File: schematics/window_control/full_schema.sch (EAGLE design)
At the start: 70 parts, among them IC1 MEGA32-P, J1 MTR-SERVO-FS5103B, J2 J2, J3 J2, J4 J2, J5 J2, J6 J2, J7 J2, J8 J2, J9 J2, Q1 2N3904, Q2 2N3904, Q3 2N3906BU, Q4 2N3904, Q5 STP14NM50N, SW1 SWITCH, U1 ESP32, U2 LM311P, U3 NE555P, U4 SN74LS32N, U5 BMP280 / 5V, U7 VOLTAGE_REGULATOR, U8 GY-SGP30, U9 LM358, X1 HC-49S (16MHZ)

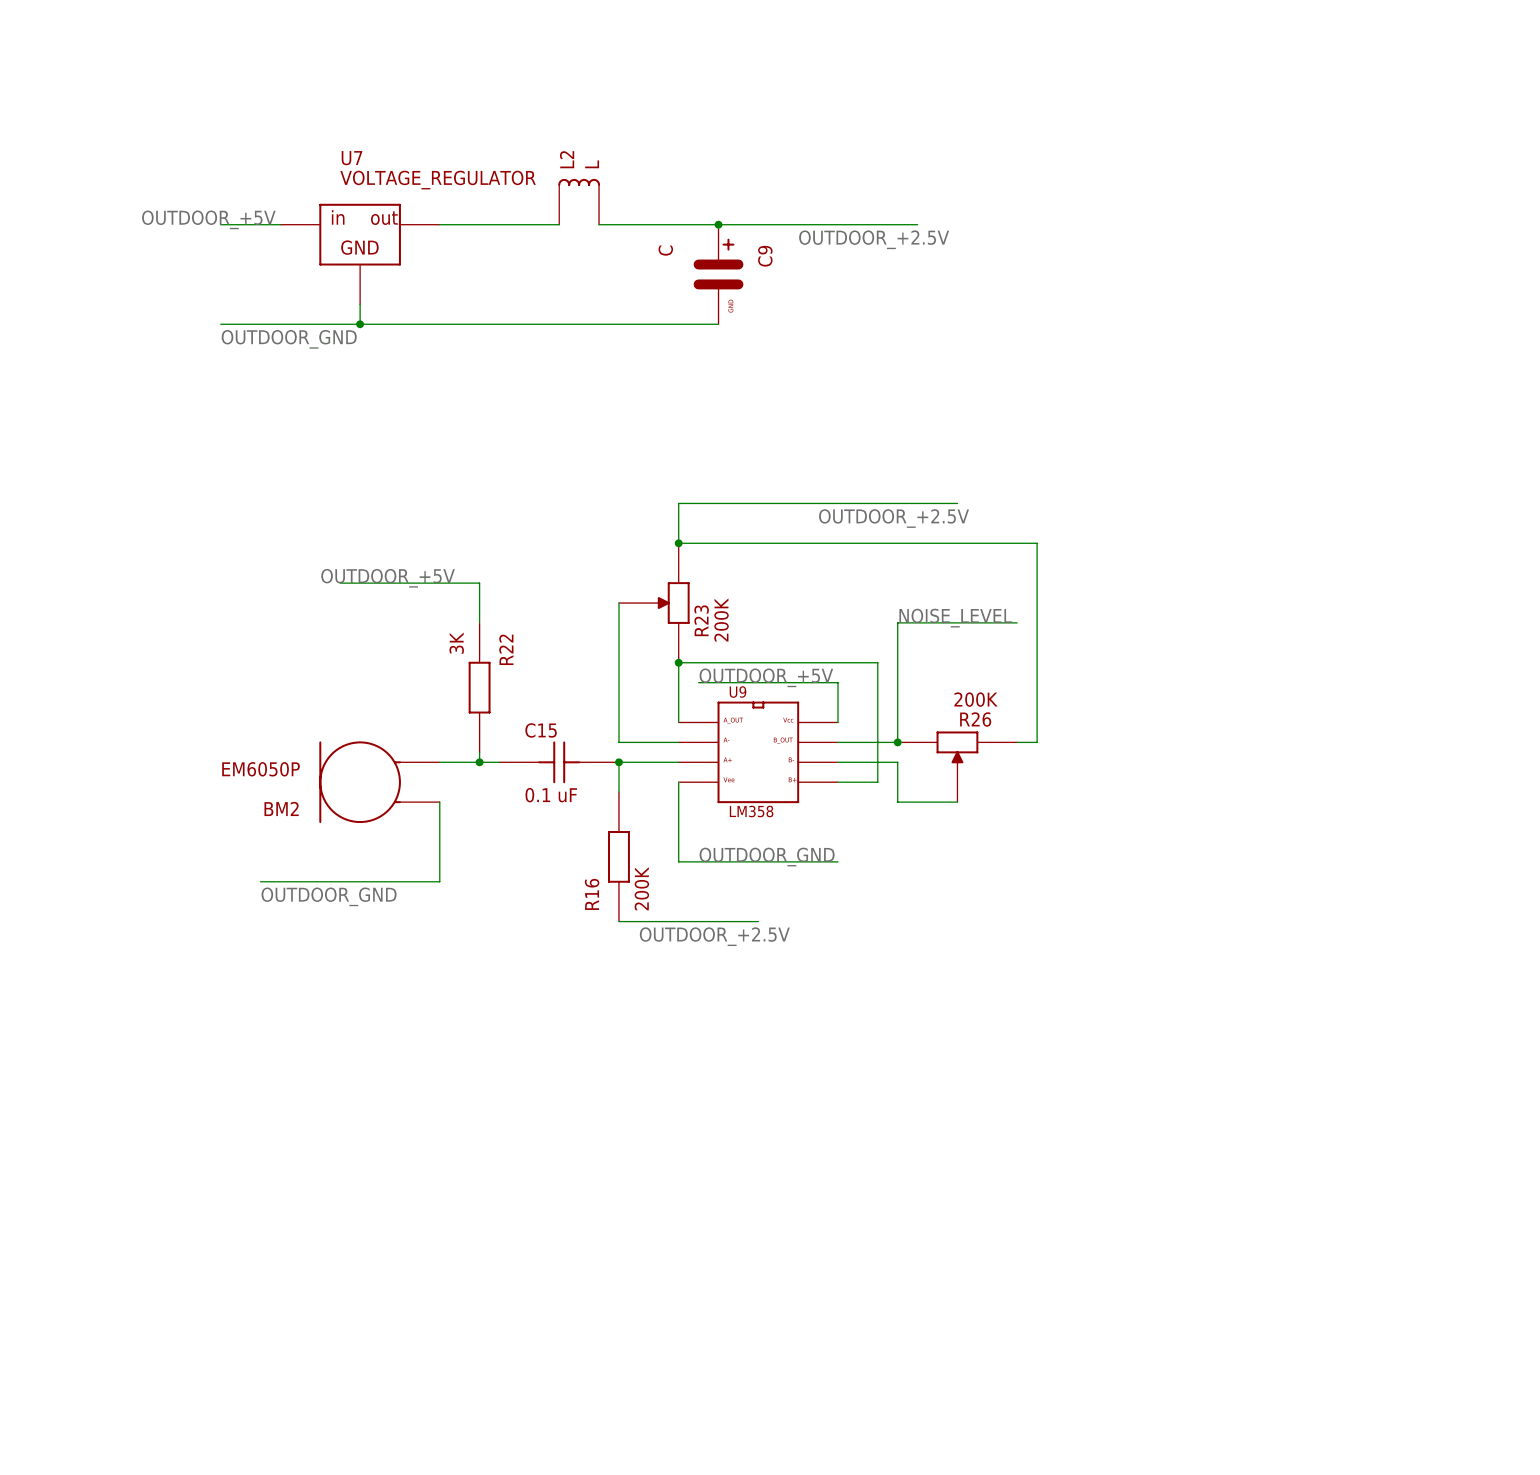
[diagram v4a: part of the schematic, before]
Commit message: Change noise sensor schema
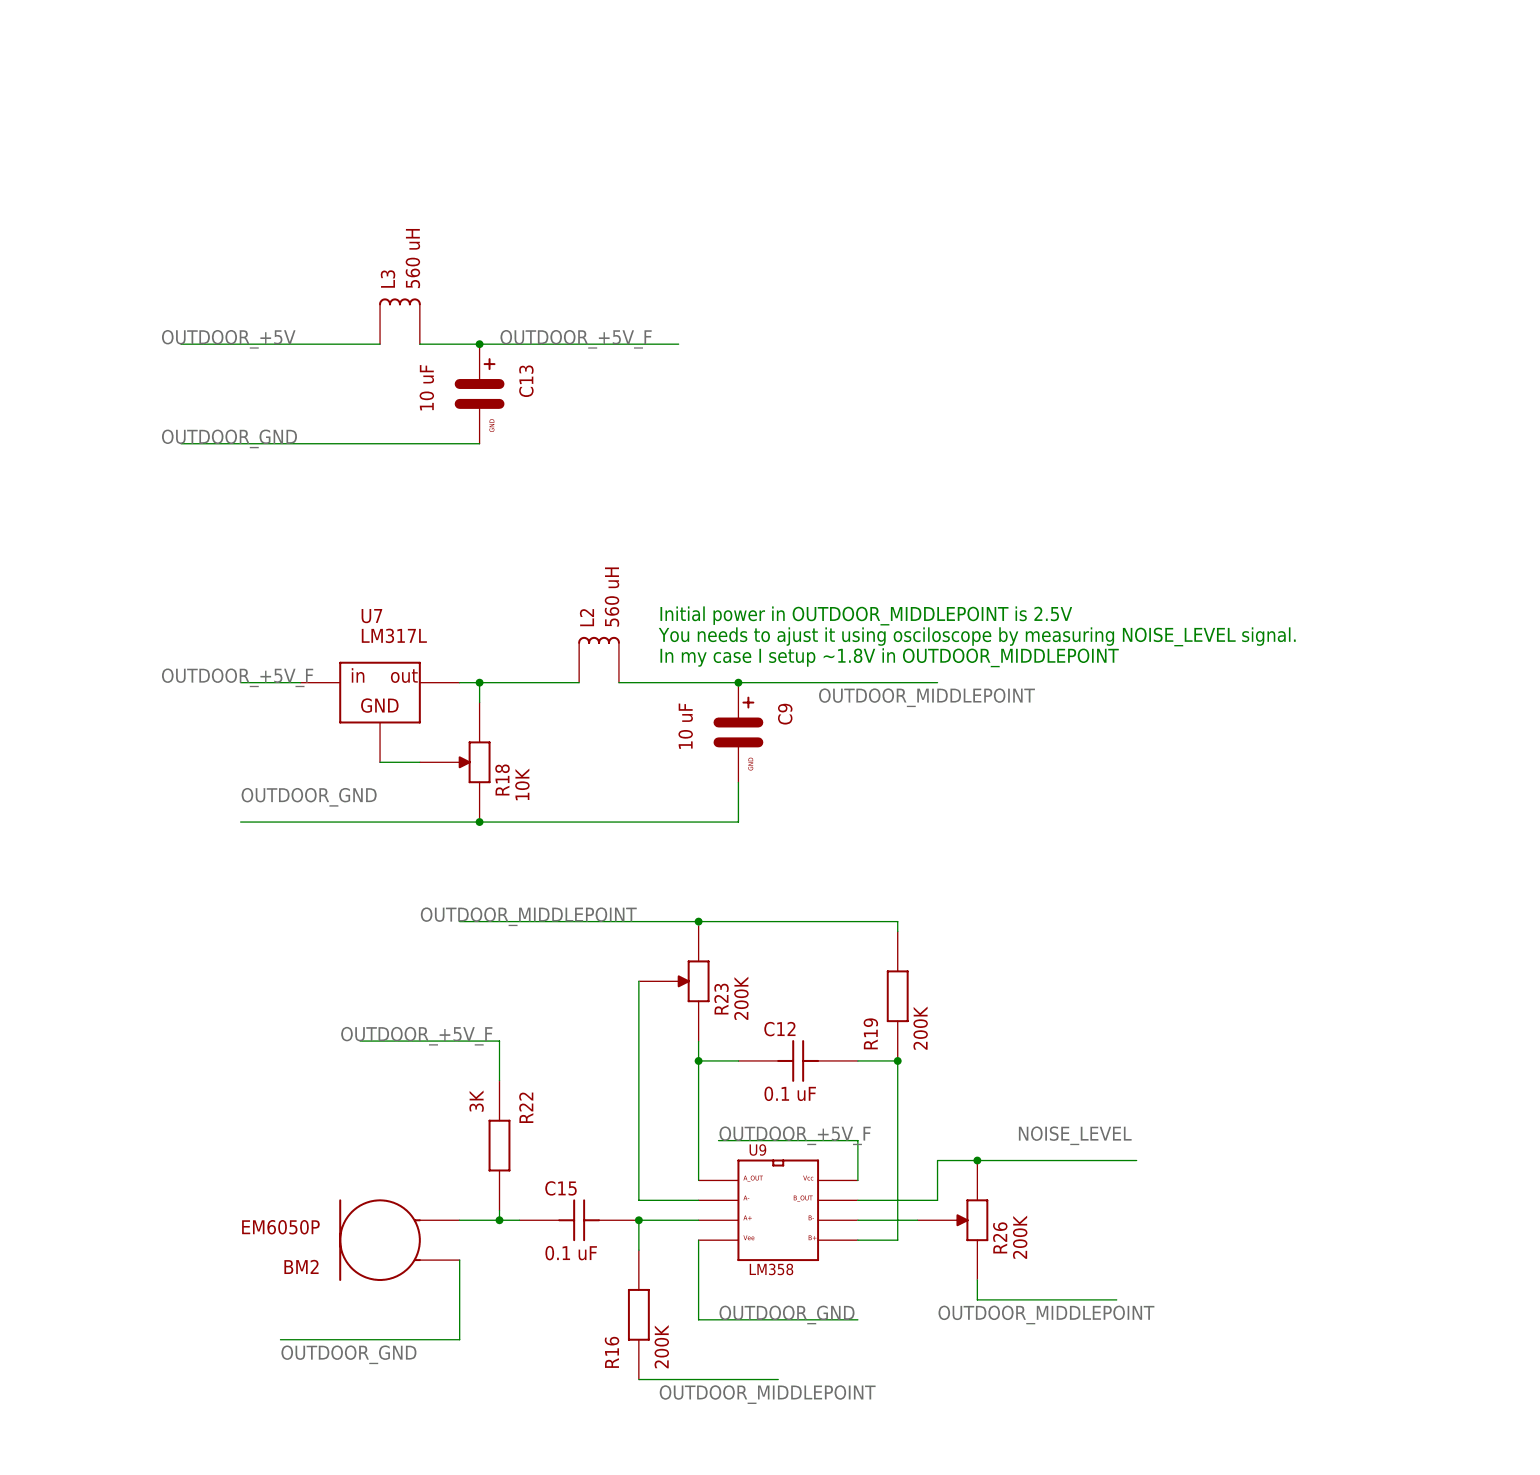
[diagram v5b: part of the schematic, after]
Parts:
- added C12: 0.1 uF, my_devices:C-1
- added C13: 10 uF, my_devices:C
- added L3: 560 uH, my_devices:L
- added R18: 10K, my_devices:RD
- added R19: 200K, my_devices:R
- C9: value C -> 10 uF
- L2: value L -> 560 uH
- U7: value VOLTAGE_REGULATOR -> LM317L
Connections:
- removed net OUTDOOR_+2.5V: C9.PIN_PLUS, L2.P$2, R16.P$1, R23.P2, R26.P1
- new net N$17: R18.P3, U7.GND
- new net N$18: C12.P$1, R23.P1, U9.A_OUT
- new net OUTDOOR_+5V_F: C13.PIN_PLUS, L3.P$2, R22.P$1, U7.IN, U9.VCC
- new net OUTDOOR_MIDDLEPOINT: C9.PIN_PLUS, L2.P$2, R16.P$1, R19.P$2, R23.P2, R26.P1
- net N$20: now also C12.P$2, R19.P$1; no longer R23.P1, U9.A_OUT
- net OUT: now also R18.P2
- net OUTDOOR_+5V: now also L3.P$1; no longer R22.P$1, U7.IN, U9.VCC
- net OUTDOOR_GND: now also C13.PIN_GND, R18.P1; no longer U7.GND
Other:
- note added: "Initial power in OUTDOOR_MIDDLEPOINT is 2.5V You needs to ajust it using osciloscope by measuring NOISE_LEVEL signal. In my case I setup ~1.8V in OUTDOOR_MIDDLEPOINT"
- moved on the sheet: BM2, C15, C9, L2, R16, R22, R23, R26, U7, U9

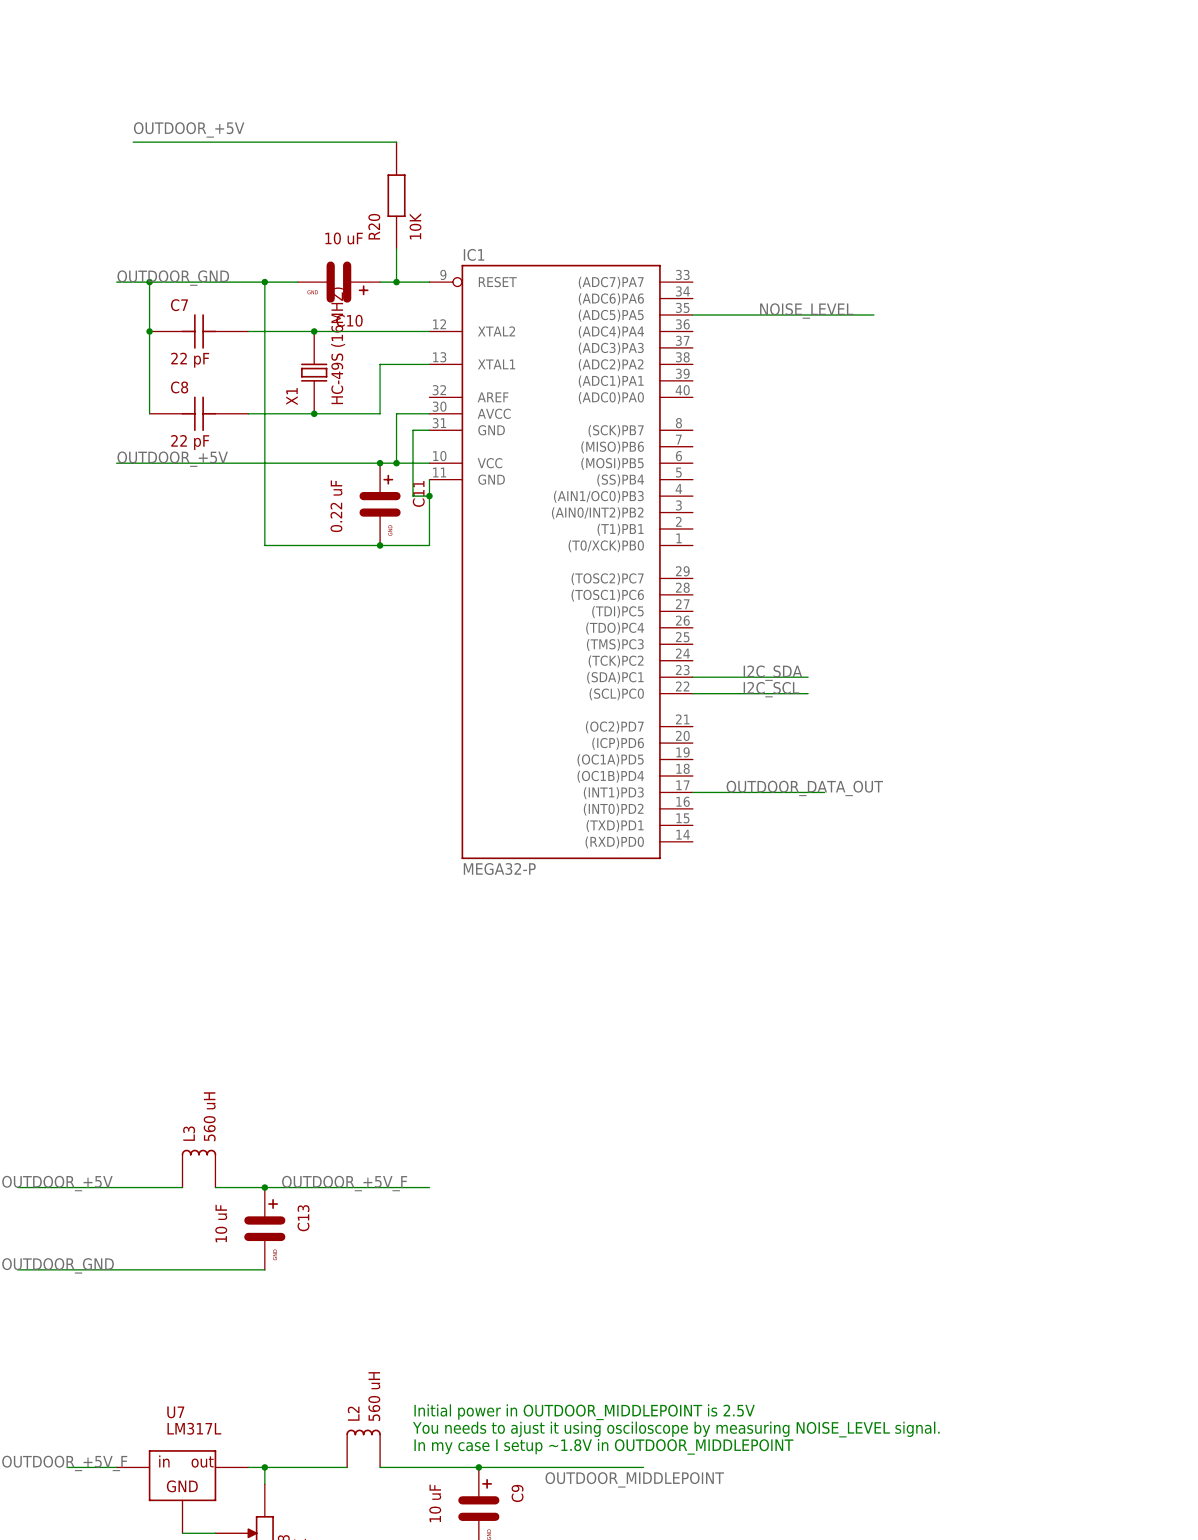
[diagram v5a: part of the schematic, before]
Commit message: changed microcontroller to ATMEGA328P to reduce device size
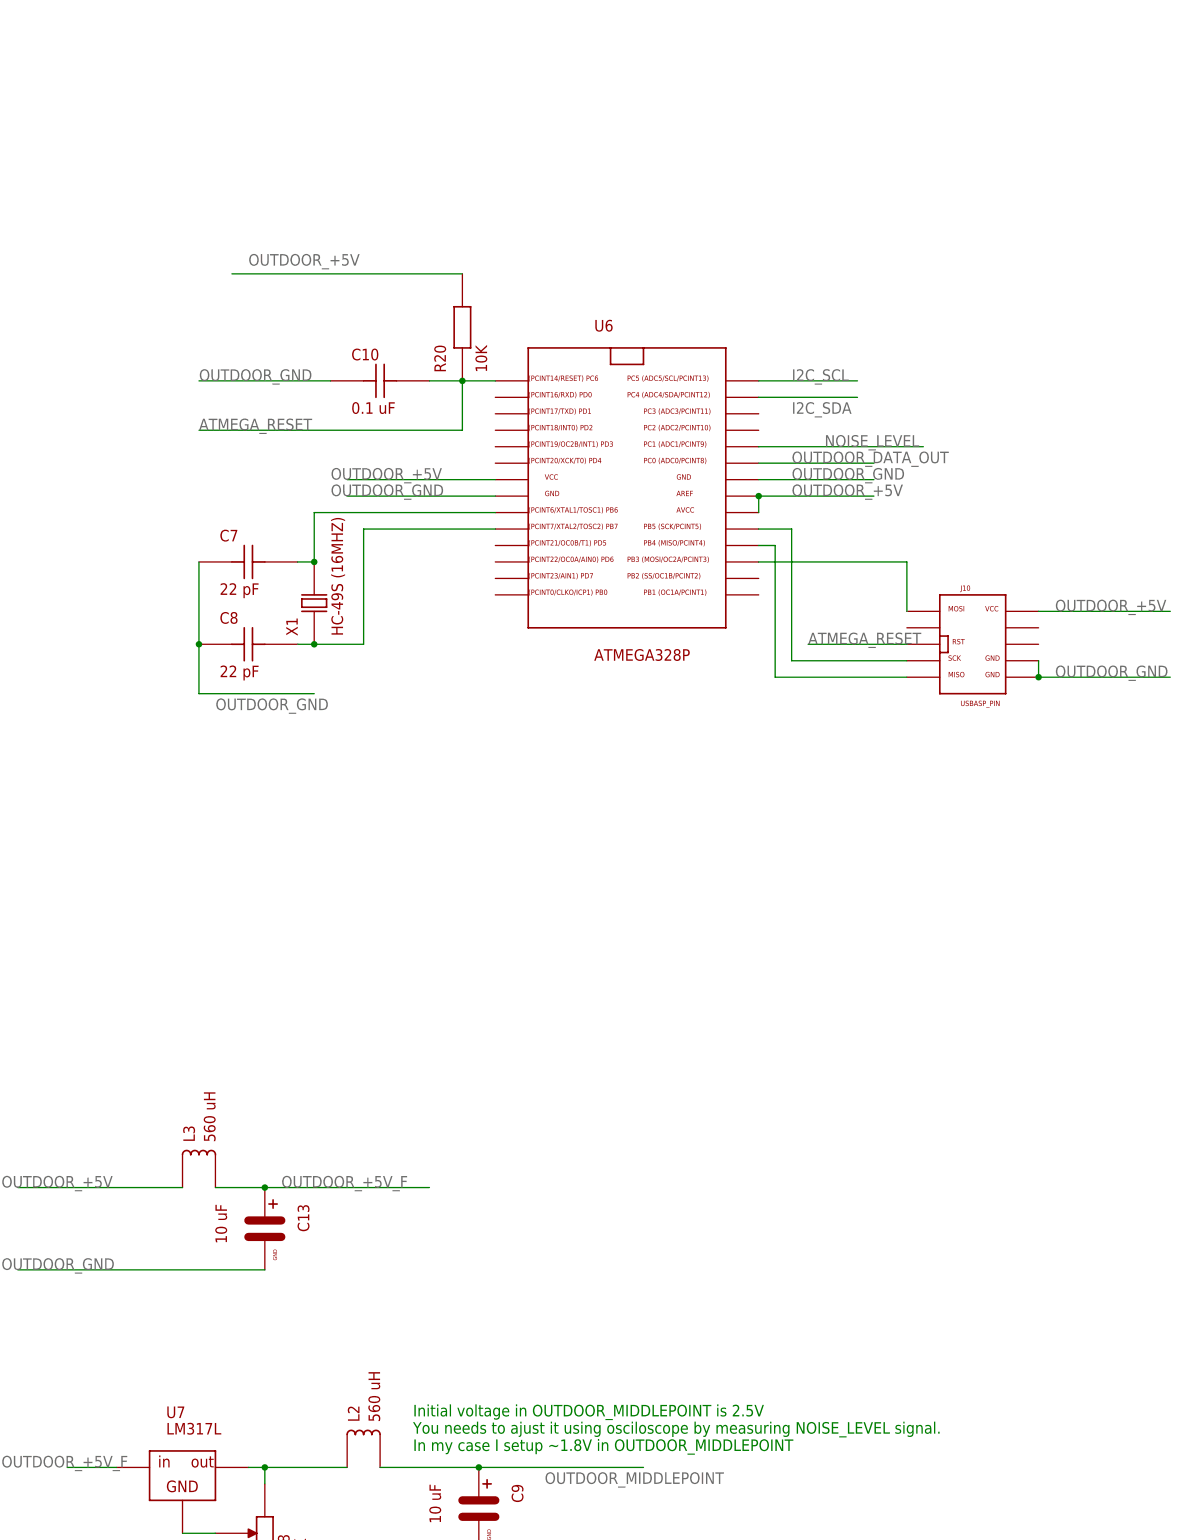
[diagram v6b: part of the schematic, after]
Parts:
- removed C11: 0.22 uF, my_devices:C
- removed IC1: MEGA32-P, atmel:MEGA32-P
- added J10: USBASP_PIN, my_devices:USBASP_PIN
- added U6: ATMEGA328P, my_devices:ATMEGA328P
- C10: value 10 uF -> 0.1 uF; device my_devices:C -> my_devices:C-1
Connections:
- removed net N$16: C10.PIN_PLUS, IC1.RESET, R20.P$1
- new net ATMEGA_RESET: C10.P$2, J10.RESET, R20.P$1, U6.PC6
- new net N$22: C7.P$2, U6.PB6, X1.P$2
- new net N$23: C8.P$2, U6.PB7, X1.P$1
- new net N$25: J10.MISO, U6.PB4
- net I2C_SCL: now also U6.PC5; no longer IC1.(SCL)PC0
- net I2C_SDA: now also U6.PC4; no longer IC1.(SDA)PC1
- net N$24: now also J10.MOSI, U6.PB3; no longer C7.P$2, IC1.XTAL2, X1.P$2
- net N$26: now also J10.SCK, U6.PB5; no longer C8.P$2, IC1.XTAL1, X1.P$1
- net NOISE_LEVEL: now also U6.PC1; no longer IC1.(ADC5)PA5
- net OUTDOOR_+5V: now also J10.VCC, U6.AREF, U6.AVCC, U6.VCC; no longer C11.PIN_PLUS, IC1.AVCC, IC1.VCC
- net OUTDOOR_DATA_OUT: now also U6.PC0; no longer IC1.(INT1)PD3
- net OUTDOOR_GND: now also C10.P$1, J10.GND, J10.GND1, U6.GND, U6.GND1; no longer C10.PIN_GND, C11.PIN_GND, IC1.GND, IC1.GND@1
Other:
- note added: "Initial voltage in OUTDOOR_MIDDLEPOINT is 2.5V You needs to ajust it using osciloscope by measuring NOISE_LEVEL signal. In my case I setup ~1.8V in OUTDOOR_MIDDLEPOINT"
- note removed: "Initial power in OUTDOOR_MIDDLEPOINT is 2.5V You needs to ajust it using osciloscope by measuring NOISE_LEVEL signal. In my case I setup ~1.8V in OUTDOOR_MIDDLEPOINT"
- moved on the sheet: C7, C8, R20, X1
